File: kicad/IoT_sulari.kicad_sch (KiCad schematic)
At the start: 14 parts, among them U2 NRF9160-SICA-B1A-R

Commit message: added status leds
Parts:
- added D1: RED, symbol Device:LED
- added D2: GREEN, symbol Device:LED
- added R5, R6: 1.5k, symbol Device:R
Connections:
- net GND: now also R5.2, R6.2
- net STATUS_LED_RED: now reaches U2.95 (P0-00)
- net STATUS_LED_RED: now also D1.2 (A)
- net STATUS_LED_GREEN: now reaches U2.96 (P0-01)
- net STATUS_LED_GREEN: now also D2.2 (A)
- new net: D2.1 (K), R6.1
- new net: D1.1 (K), R5.1
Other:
- title: (none) -> IoT sensor
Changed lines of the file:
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@@
   (paper "A4")
   (title_block
+    (title "IoT sensor")
     (company "University of Oulu")
   )
@@
     (stroke (width 0) (type default))
   )
+  (wire (pts (xy 262.89 146.05) (xy 262.89 149.86))
+    (stroke (width 0) (type default))
+  )
   (wire (pts (xy 20.32 177.8) (xy 25.4 177.8))
     (stroke (width 0) (type default))
@@
     (stroke (width 0) (type default))
   )
+  (wire (pts (xy 273.05 157.48) (xy 273.05 158.75))
+    (stroke (width 0) (type default))
+  )
   (wire (pts (xy 20.32 175.26) (xy 25.4 175.26))
     (stroke (width 0) (type default))
@@
     (stroke (width 0) (type default))
   )
+  (wire (pts (xy 262.89 157.48) (xy 262.89 158.75))
+    (stroke (width 0) (type default))
+  )
   (wire (pts (xy 20.32 116.84) (xy 25.4 116.84))
     (stroke (width 0) (type default))
@@
   )
   (wire (pts (xy 20.32 177.8) (xy 20.32 175.26))
+    (stroke (width 0) (type default))
+  )
+  (wire (pts (xy 273.05 146.05) (xy 273.05 149.86))
     (stroke (width 0) (type default))
   )
@@
     )
   )
+  (global_label "STATUS_LED_GREEN" (shape input) (at 273.05 138.43 90) (fields_autoplaced)
+    (effects (font (size 1.27 1.27)) (justify left))
+    (property "Intersheetrefs" "${INTERSHEET_REFS}" (at 273.05 117.2001 90)
+      (effects (font (size 1.27 1.27)) (justify left) hide)
+    )
+  )
+  (global_label "STATUS_LED_GREEN" (shape input) (at 139.7 74.93 180) (fields_autoplaced)
+    (effects (font (size 1.27 1.27)) (justify right))
+    (property "Intersheetrefs" "${INTERSHEET_REFS}" (at 118.4701 74.93 0)
+      (effects (font (size 1.27 1.27)) (justify right) hide)
+    )
+  )
+  (global_label "STATUS_LED_RED" (shape input) (at 262.89 138.43 90) (fields_autoplaced)
+    (effects (font (size 1.27 1.27)) (justify left))
+    (property "Intersheetrefs" "${INTERSHEET_REFS}" (at 262.89 119.6796 90)
+      (effects (font (size 1.27 1.27)) (justify left) hide)
+    )
+  )
   (global_label "SIM_RST" (shape input) (at 222.25 83.82 0) (fields_autoplaced)
     (effects (font (size 1.27 1.27)) (justify left))
@@
     (property "Intersheetrefs" "${INTERSHEET_REFS}" (at 231.3244 76.2 0)
       (effects (font (size 1.27 1.27)) (justify left) hide)
+    )
+  )
+  (global_label "STATUS_LED_RED" (shape input) (at 139.7 72.39 180) (fields_autoplaced)
+    (effects (font (size 1.27 1.27)) (justify right))
+    (property "Intersheetrefs" "${INTERSHEET_REFS}" (at 120.9496 72.39 0)
+      (effects (font (size 1.27 1.27)) (justify right) hide)
     )
   )
@@
     )
   )
+  (symbol (lib_id "Device:LED") (at 273.05 142.24 90) (unit 1)
+    (in_bom yes) (on_board yes) (dnp no) (fields_autoplaced)
+    (property "Reference" "D2" (at 276.86 143.1925 90)
+      (effects (font (size 1.27 1.27)) (justify right))
+    )
+    (property "Value" "GREEN" (at 276.86 145.7325 90)
+      (effects (font (size 1.27 1.27)) (justify right))
+    )
+    (property "Footprint" "" (at 273.05 142.24 0)
+      (effects (font (size 1.27 1.27)) hide)
+    )
+    (property "Datasheet" "~" (at 273.05 142.24 0)
+      (effects (font (size 1.27 1.27)) hide)
+    )
+    (pin "1")
+    (pin "2")
+    (instances
+      (project "IoT_sulari"
+        (path "/184b47ed-2c2b-4c02-be35-d18f4f4e5685"
+          (reference "D2") (unit 1)
+        )
+      )
+    )
+  )
   (symbol (lib_id "power:+3.3V") (at 110.49 31.75 0) (unit 1)
     (in_bom yes) (on_board yes) (dnp no) (fields_autoplaced)
@@
     )
   )
+  (symbol (lib_id "Device:R") (at 262.89 153.67 0) (unit 1)
+    (in_bom yes) (on_board yes) (dnp no) (fields_autoplaced)
+    (property "Reference" "R5" (at 265.43 153.035 0)
+      (effects (font (size 1.27 1.27)) (justify left))
+    )
+    (property "Value" "1.5k" (at 265.43 155.575 0)
+      (effects (font (size 1.27 1.27)) (justify left))
+    )
+    (property "Footprint" "" (at 261.112 153.67 90)
+      (effects (font (size 1.27 1.27)) hide)
+    )
+    (property "Datasheet" "~" (at 262.89 153.67 0)
+      (effects (font (size 1.27 1.27)) hide)
+    )
+    (pin "1")
+    (pin "2")
+    (instances
+      (project "IoT_sulari"
+        (path "/184b47ed-2c2b-4c02-be35-d18f4f4e5685"
+          (reference "R5") (unit 1)
+        )
+      )
+    )
+  )
   (symbol (lib_id "Device:C") (at 120.65 39.37 0) (unit 1)
     (in_bom yes) (on_board yes) (dnp no) (fields_autoplaced)
@@
     )
   )
+  (symbol (lib_id "Device:LED") (at 262.89 142.24 90) (unit 1)
+    (in_bom yes) (on_board yes) (dnp no) (fields_autoplaced)
+    (property "Reference" "D1" (at 266.7 143.1925 90)
+      (effects (font (size 1.27 1.27)) (justify right))
+    )
+    (property "Value" "RED" (at 266.7 145.7325 90)
+      (effects (font (size 1.27 1.27)) (justify right))
+    )
+    (property "Footprint" "" (at 262.89 142.24 0)
+      (effects (font (size 1.27 1.27)) hide)
+    )
+    (property "Datasheet" "~" (at 262.89 142.24 0)
+      (effects (font (size 1.27 1.27)) hide)
+    )
+    (pin "1")
+    (pin "2")
+    (instances
+      (project "IoT_sulari"
+        (path "/184b47ed-2c2b-4c02-be35-d18f4f4e5685"
+          (reference "D1") (unit 1)
+        )
+      )
+    )
+  )
   (symbol (lib_id "Device:C") (at 130.81 39.37 0) (unit 1)
     (in_bom yes) (on_board yes) (dnp no) (fields_autoplaced)
@@
     )
   )
+  (symbol (lib_id "power:GND") (at 273.05 158.75 0) (unit 1)
+    (in_bom yes) (on_board yes) (dnp no) (fields_autoplaced)
+    (property "Reference" "#PWR024" (at 273.05 165.1 0)
+      (effects (font (size 1.27 1.27)) hide)
+    )
+    (property "Value" "GND" (at 273.05 163.83 0)
+      (effects (font (size 1.27 1.27)))
+    )
+    (property "Footprint" "" (at 273.05 158.75 0)
+      (effects (font (size 1.27 1.27)) hide)
+    )
+    (property "Datasheet" "" (at 273.05 158.75 0)
+      (effects (font (size 1.27 1.27)) hide)
+    )
+    (pin "1")
+    (instances
+      (project "IoT_sulari"
+        (path "/184b47ed-2c2b-4c02-be35-d18f4f4e5685"
+          (reference "#PWR024") (unit 1)
+        )
+      )
+    )
+  )
   (symbol (lib_id "Device:C") (at 158.75 142.24 0) (unit 1)
     (in_bom yes) (on_board yes) (dnp no) (fields_autoplaced)
@@
         )
       )
+    )
+  )
+  (symbol (lib_id "power:GND") (at 262.89 158.75 0) (unit 1)
+    (in_bom yes) (on_board yes) (dnp no) (fields_autoplaced)
+    (property "Reference" "#PWR023" (at 262.89 165.1 0)
+      (effects (font (size 1.27 1.27)) hide)
+    )
+    (property "Value" "GND" (at 262.89 163.83 0)
+      (effects (font (size 1.27 1.27)))
+    )
+    (property "Footprint" "" (at 262.89 158.75 0)
+      (effects (font (size 1.27 1.27)) hide)
+    )
+    (property "Datasheet" "" (at 262.89 158.75 0)
+      (effects (font (size 1.27 1.27)) hide)
+    )
+    (pin "1")
+    (instances
+      (project "IoT_sulari"
+        (path "/184b47ed-2c2b-4c02-be35-d18f4f4e5685"
+          (reference "#PWR023") (unit 1)
+        )
+      )
+    )
+  )
+  (symbol (lib_id "Device:R") (at 273.05 153.67 0) (unit 1)
+    (in_bom yes) (on_board yes) (dnp no) (fields_autoplaced)
+    (property "Reference" "R6" (at 275.59 153.035 0)
+      (effects (font (size 1.27 1.27)) (justify left))
+    )
+    (property "Value" "1.5k" (at 275.59 155.575 0)
+      (effects (font (size 1.27 1.27)) (justify left))
+    )
+    (property "Footprint" "" (at 271.272 153.67 90)
+      (effects (font (size 1.27 1.27)) hide)
+    )
+    (property "Datasheet" "~" (at 273.05 153.67 0)
+      (effects (font (size 1.27 1.27)) hide)
+    )
+    (pin "1")
+    (pin "2")
+    (instances
+      (project "IoT_sulari"
+        (path "/184b47ed-2c2b-4c02-be35-d18f4f4e5685"
+          (reference "R6") (unit 1)
+        )
+      )

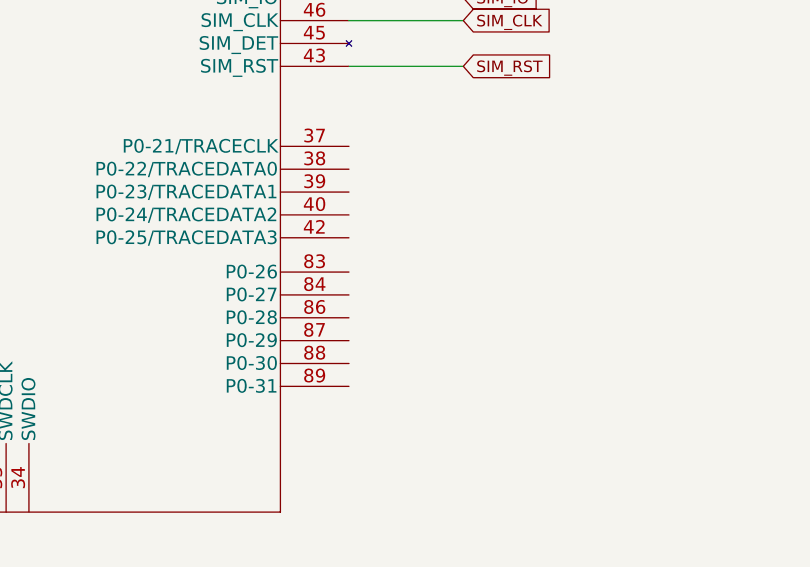
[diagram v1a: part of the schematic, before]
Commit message: sensorboard schema + esd datasheet
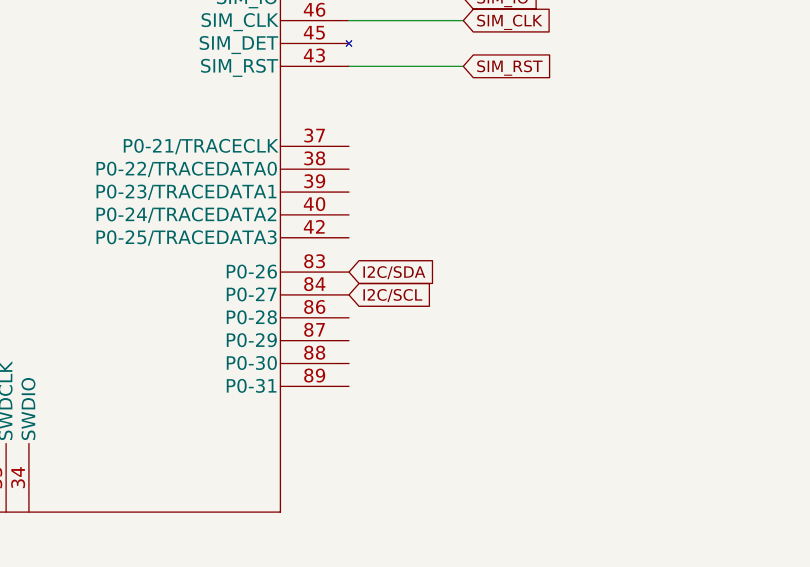
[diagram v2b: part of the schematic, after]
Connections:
- net I2C/SDA: now reaches U2.83 (P0-26)
- net I2C/SCL: now reaches U2.84 (P0-27)
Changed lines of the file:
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@@
+    )
+  )
+  (global_label "I2C{slash}SCL" (shape input) (at 209.55 109.22 0) (fields_autoplaced)
+    (effects (font (size 1.27 1.27)) (justify left))
+    (property "Intersheetrefs" "${INTERSHEET_REFS}" (at 220.3782 109.22 0)
+      (effects (font (size 1.27 1.27)) (justify left) hide)
     )
   )
@@
       (effects (font (size 1.27 1.27)) (justify left) hide)
     )
+  )
+  (global_label "I2C{slash}SDA" (shape input) (at 209.55 106.68 0) (fields_autoplaced)
+    (effects (font (size 1.27 1.27)) (justify left))
+    (property "Intersheetrefs" "${INTERSHEET_REFS}" (at 220.4387 106.68 0)
+      (effects (font (size 1.27 1.27)) (justify left) hide)
+    )

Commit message: added comments and muokkasin komponenttiennumeroinnin selvemmäksi.
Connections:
- net +3.3V: now also C4.1, C5.1, U2.12 (VDD_GPIO)
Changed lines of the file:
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@@
   (junction (at 20.32 127) (diameter 0) (color 0 0 0 0)
   )
+  (junction (at 105.41 49.53) (diameter 0) (color 0 0 0 0)
+  )
   (junction (at 20.32 160.02) (diameter 0) (color 0 0 0 0)
   )
@@
   )
   (wire (pts (xy 20.32 162.56) (xy 20.32 160.02))
+    (stroke (width 0) (type default))
+  )
+  (wire (pts (xy 105.41 48.26) (xy 105.41 49.53))
     (stroke (width 0) (type default))
   )
@@
         )
       )
+    )
+  )
+  (symbol (lib_id "power:+3.3V") (at 105.41 48.26 0) (unit 1)
+    (in_bom yes) (on_board yes) (dnp no) (fields_autoplaced)
+    (property "Reference" "#PWR025" (at 105.41 52.07 0)
+      (effects (font (size 1.27 1.27)) hide)
+    )
+    (property "Value" "+3.3V" (at 105.41 44.45 0)
+      (effects (font (size 1.27 1.27)))
+    )
+    (property "Footprint" "" (at 105.41 48.26 0)
+      (effects (font (size 1.27 1.27)) hide)
+    )
+    (property "Datasheet" "" (at 105.41 48.26 0)
+      (effects (font (size 1.27 1.27)) hide)
+    )
+    (pin "1")
+    (instances
+      (project "IoT_sulari"
+        (path "/184b47ed-2c2b-4c02-be35-d18f4f4e5685"
+          (reference "#PWR025") (unit 1)
+        )
+      )

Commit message: nreset
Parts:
- added SW1: SW_SPST, symbol Switch:SW_SPST
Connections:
- net GND: now also SW1.1 (A)
- net nreset: no longer names the net of R2.2
- net nreset: now also SW1.2 (B)
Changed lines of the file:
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@@
   (junction (at 20.32 121.92) (diameter 0) (color 0 0 0 0)
   )
+  (junction (at 158.75 157.48) (diameter 0) (color 0 0 0 0)
+  )
   (junction (at 20.32 86.36) (diameter 0) (color 0 0 0 0)
   )
@@
     (stroke (width 0) (type default))
   )
-  (wire (pts (xy 168.91 146.05) (xy 168.91 147.32))
-    (stroke (width 0) (type default))
-  )
   (wire (pts (xy 110.49 31.75) (xy 110.49 34.29))
     (stroke (width 0) (type default))
@@
     (stroke (width 0) (type default))
   )
+  (wire (pts (xy 158.75 146.05) (xy 158.75 157.48))
+    (stroke (width 0) (type default))
+  )
   (wire (pts (xy 20.32 177.8) (xy 20.32 175.26))
     (stroke (width 0) (type default))
@@
     (stroke (width 0) (type default))
   )
+  (wire (pts (xy 158.75 157.48) (xy 168.91 157.48))
+    (stroke (width 0) (type default))
+  )
   (wire (pts (xy 20.32 86.36) (xy 25.4 86.36))
     (stroke (width 0) (type default))
@@
     (stroke (width 0) (type default))
   )
-  (wire (pts (xy 158.75 146.05) (xy 158.75 148.59))
-    (stroke (width 0) (type default))
-  )
   (wire (pts (xy 20.32 109.22) (xy 25.4 109.22))
     (stroke (width 0) (type default))
@@
     (stroke (width 0) (type default))
   )
+  (wire (pts (xy 168.91 156.21) (xy 168.91 157.48))
+    (stroke (width 0) (type default))
+  )
   (wire (pts (xy 20.32 180.34) (xy 25.4 180.34))
     (stroke (width 0) (type default))
@@
   )
   (wire (pts (xy 83.82 24.13) (xy 83.82 25.4))
+    (stroke (width 0) (type default))
+  )
+  (wire (pts (xy 158.75 157.48) (xy 158.75 158.75))
     (stroke (width 0) (type default))
   )
@@
     (property "Intersheetrefs" "${INTERSHEET_REFS}" (at 232.9572 78.74 0)
       (effects (font (size 1.27 1.27)) (justify left) hide)
-    )
-  )
-  (global_label "nreset" (shape input) (at 168.91 147.32 270) (fields_autoplaced)
-    (effects (font (size 1.27 1.27)) (justify right))
-    (property "Intersheetrefs" "${INTERSHEET_REFS}" (at 168.91 156.092 90)
-      (effects (font (size 1.27 1.27)) (justify right) hide)
     )
   )
@@
     )
   )
+  (symbol (lib_id "Switch:SW_SPST") (at 168.91 151.13 90) (unit 1)
+    (in_bom yes) (on_board yes) (dnp no) (fields_autoplaced)
+    (property "Reference" "SW1" (at 170.18 150.495 90)
+      (effects (font (size 1.27 1.27)) (justify right))
+    )
+    (property "Value" "SW_SPST" (at 170.18 153.035 90)
+      (effects (font (size 1.27 1.27)) (justify right))
+    )
+    (property "Footprint" "" (at 168.91 151.13 0)
+      (effects (font (size 1.27 1.27)) hide)
+    )
+    (property "Datasheet" "~" (at 168.91 151.13 0)
+      (effects (font (size 1.27 1.27)) hide)
+    )
+    (pin "1")
+    (pin "2")
+    (instances
+      (project "IoT_sulari"
+        (path "/184b47ed-2c2b-4c02-be35-d18f4f4e5685"
+          (reference "SW1") (unit 1)
+        )
+      )
+    )
+  )
   (symbol (lib_id "power:GND") (at 130.81 44.45 0) (unit 1)
     (in_bom yes) (on_board yes) (dnp no) (fields_autoplaced)
@@
     )
   )
-  (symbol (lib_id "power:GND") (at 158.75 148.59 0) (unit 1)
-    (in_bom yes) (on_board yes) (dnp no) (fields_autoplaced)
-    (property "Reference" "#PWR016" (at 158.75 154.94 0)
-      (effects (font (size 1.27 1.27)) hide)
-    )
-    (property "Value" "GND" (at 158.75 153.67 0)
+  (symbol (lib_id "power:GND") (at 158.75 158.75 0) (unit 1)
+    (in_bom yes) (on_board yes) (dnp no) (fields_autoplaced)
+    (property "Reference" "#PWR016" (at 158.75 165.1 0)
+      (effects (font (size 1.27 1.27)) hide)
+    )
+    (property "Value" "GND" (at 158.75 163.83 0)
       (effects (font (size 1.27 1.27)))
     )
-    (property "Footprint" "" (at 158.75 148.59 0)
-      (effects (font (size 1.27 1.27)) hide)
-    )
-    (property "Datasheet" "" (at 158.75 148.59 0)
-      (effects (font (size 1.27 1.27)) hide)
-    )
+    (property "Footprint" "" (at 158.75 158.75 0)
+      (effects (font (size 1.27 1.27)) hide)
+    )
+    (property "Datasheet" "" (at 158.75 158.75 0)
+      (effects (font (size 1.27 1.27)) hide)
+    )

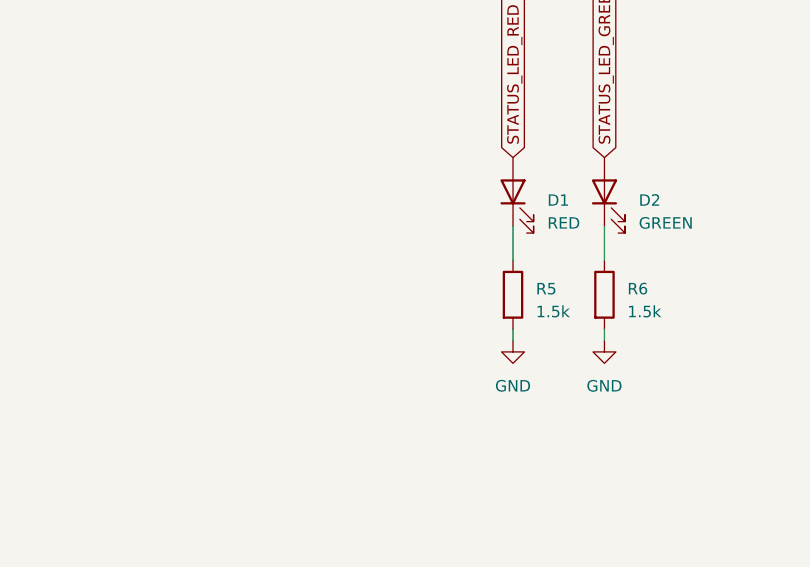
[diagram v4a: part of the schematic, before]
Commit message: added antenna connector
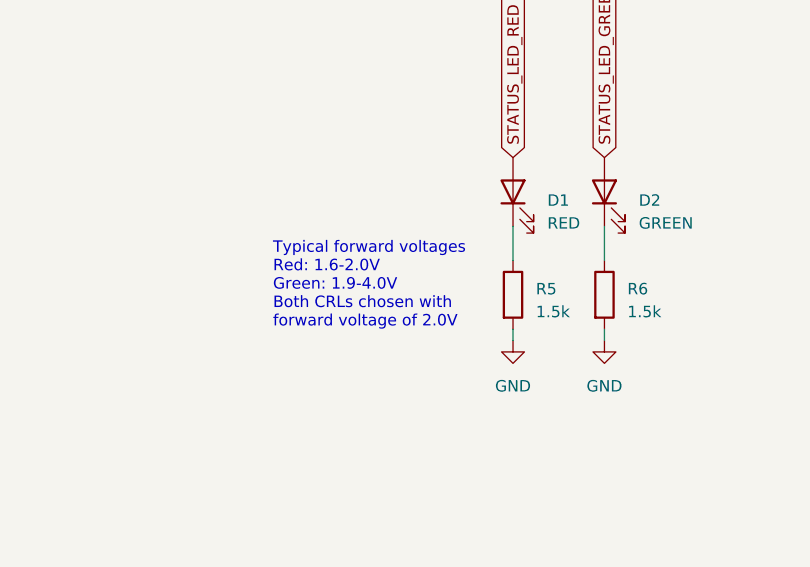
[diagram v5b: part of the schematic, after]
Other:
- note added: "Typical forward voltages Red: 1.6-2.0V Green: 1.9-4.0V Both CRLs chosen with forward voltage of 2.0V"
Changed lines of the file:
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@@
+    (effects (font (size 1.27 1.27)) (justify left bottom))
+  )
+  (text "Typical forward voltages\nRed: 1.6-2.0V\nGreen: 1.9-4.0V\nBoth CRLs chosen with\nforward voltage of 2.0V"
+    (at 236.22 157.48 0)
     (effects (font (size 1.27 1.27)) (justify left bottom))
   )
